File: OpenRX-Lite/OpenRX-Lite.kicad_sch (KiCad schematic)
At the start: 0 parts

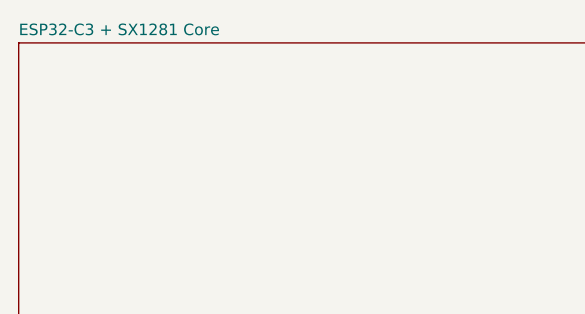
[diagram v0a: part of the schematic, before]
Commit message: OpenRX Lite (UFL + molex)
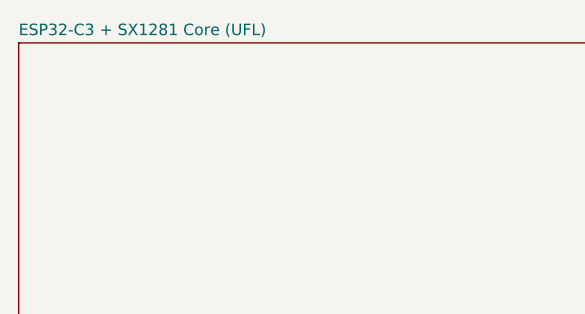
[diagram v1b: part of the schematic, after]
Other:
- sheet ESP32-C3 + SX1281 Core renamed ESP32-C3 + SX1281 Core (UFL)
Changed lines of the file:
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@@
 			(color 0 0 0 0)
 		)
-		(property "Sheetname" "ESP32-C3 + SX1281 Core"
+		(property "Sheetname" "ESP32-C3 + SX1281 Core (UFL)"
 			(at 25.4 24.6888 0)
 			(show_name no)

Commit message: annotate
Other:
- note added: "07/06/2026"
- note added: "1"
- note added: "Single ELRS radio instance"
